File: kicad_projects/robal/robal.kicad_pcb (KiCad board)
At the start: 2 copper layers, 67.6 x 40.6 mm, 52 parts, among them J1 Conn_01x08, J2 Conn_01x08, J3 Conn_02x08_Odd_Even, J4 Conn_02x05_Odd_Even, J5 Conn_02x02_Odd_Even, J6 Conn_02x02_Odd_Even, J7 Conn_02x02_Odd_Even, J8 Conn_02x02_Odd_Even, U1 NE5532DR, U2 NE5532DR

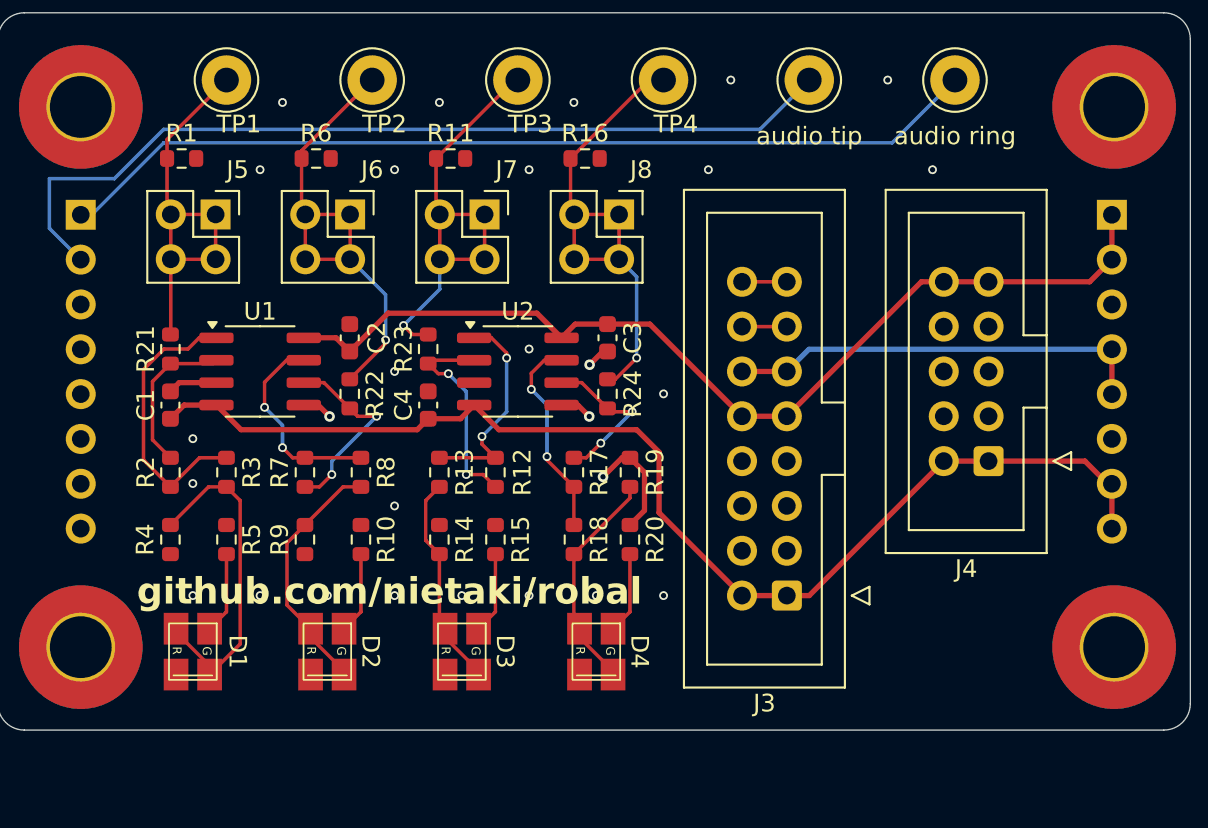
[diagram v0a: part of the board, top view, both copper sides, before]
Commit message: Better decoupling caps, red line marker, removed part designators
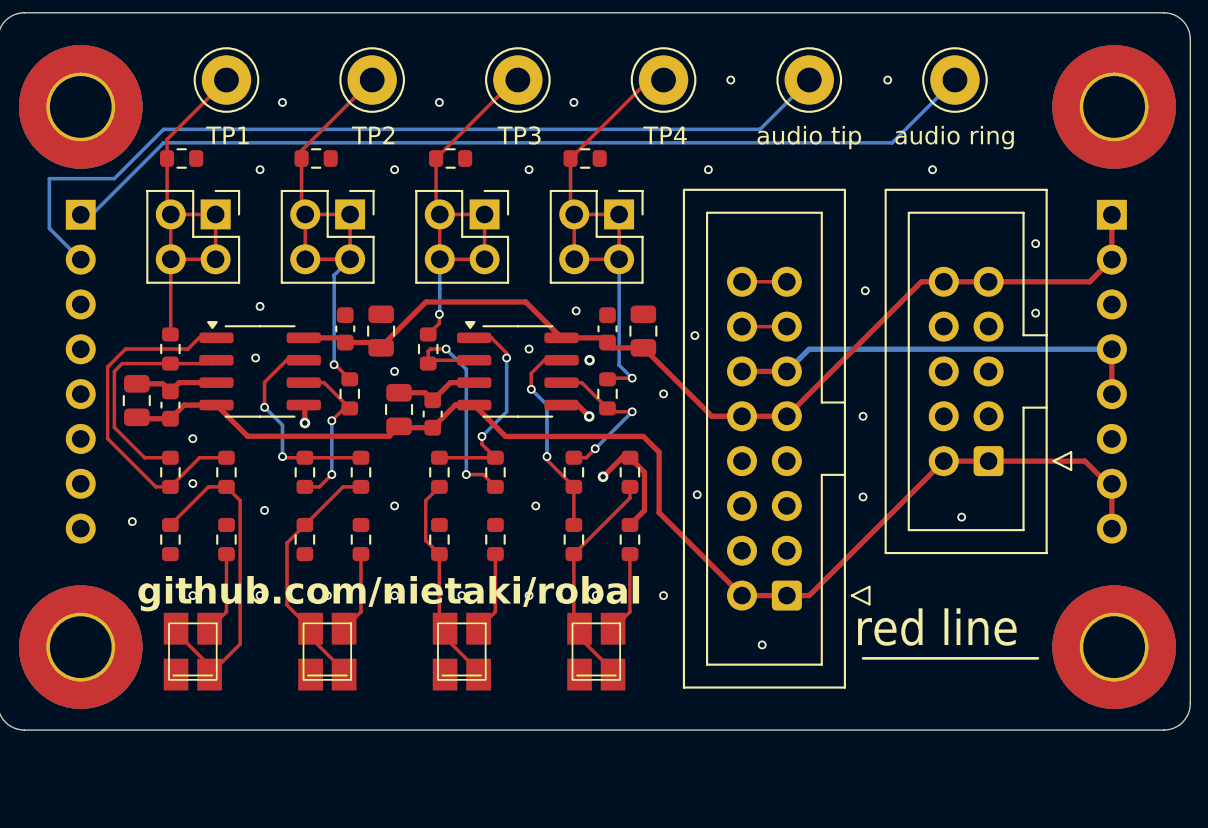
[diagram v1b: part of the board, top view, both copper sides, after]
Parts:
- added C5: 10u, Capacitor_SMD:C_0805_2012Metric, F.Cu at (164.0, 93.0)
- added C6: 10u, Capacitor_SMD:C_0805_2012Metric, F.Cu at (150.1, 97.4)
- added C7: 10u, Capacitor_SMD:C_0805_2012Metric, F.Cu at (149.1, 93.0)
- added C8: 10u, Capacitor_SMD:C_0805_2012Metric, F.Cu at (135.3, 96.9)
- moved C4 0.57 mm to (152.0, 97.7)
- moved C2 0.57 mm to (147.1, 92.8)
- moved C3 0.51 mm to (161.9, 92.8), turned to 90 degrees
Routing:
- net GND: track 14.2 -> 19.1 mm, vias 28 -> 43
- net Net-(U1A--): track 8.86 -> 13.1 mm
- net Net-(R2-Pad2): track 16.0 -> 19.5 mm
- net -12V: track 67.5 -> 69.8 mm
- net Net-(U2A--): track 12.1 -> 14.0 mm
- net Net-(U1B--): track 11.1 -> 9.38 mm
- net Net-(J7-Pin_1): track 26.1 -> 24.4 mm
- net Net-(J6-Pin_1): track 28.0 -> 27.1 mm
- added copper zone on B.Cu, net Net-(J5-Pin_1)
- added copper zone on B.Cu, net Net-(J6-Pin_1)
- added copper zone on B.Cu, net Net-(J7-Pin_1)
- added copper zone on B.Cu, net Net-(J8-Pin_1)
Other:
- board text added: "red line"
